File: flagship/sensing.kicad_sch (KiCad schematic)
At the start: 12 parts, among them Q701 2N7002, U11 INA228

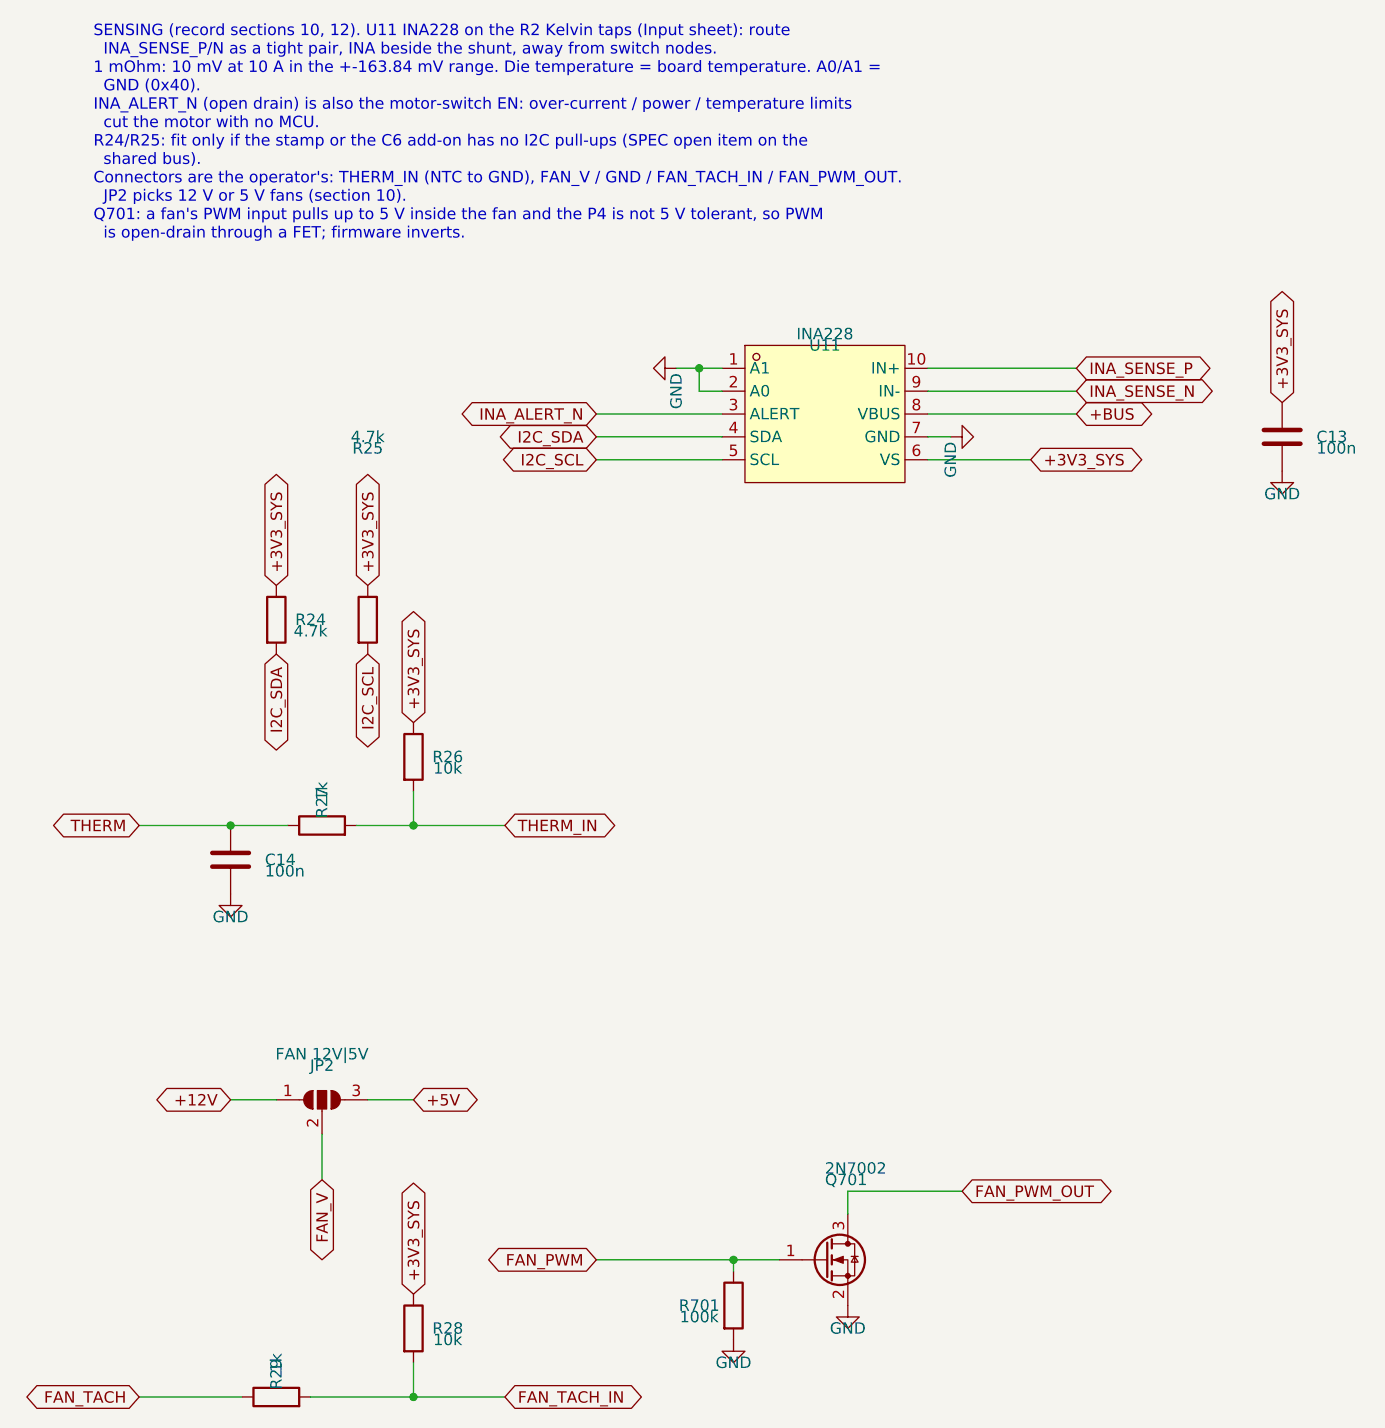
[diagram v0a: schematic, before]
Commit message: flagship: fan supply jumper defaults to 12 V (pre-bridged 1-2, cut and re-bridge for 5 V)
Co-Authored-By: Claude Opus 5.5 (1M context) <noreply@anthropic.com>
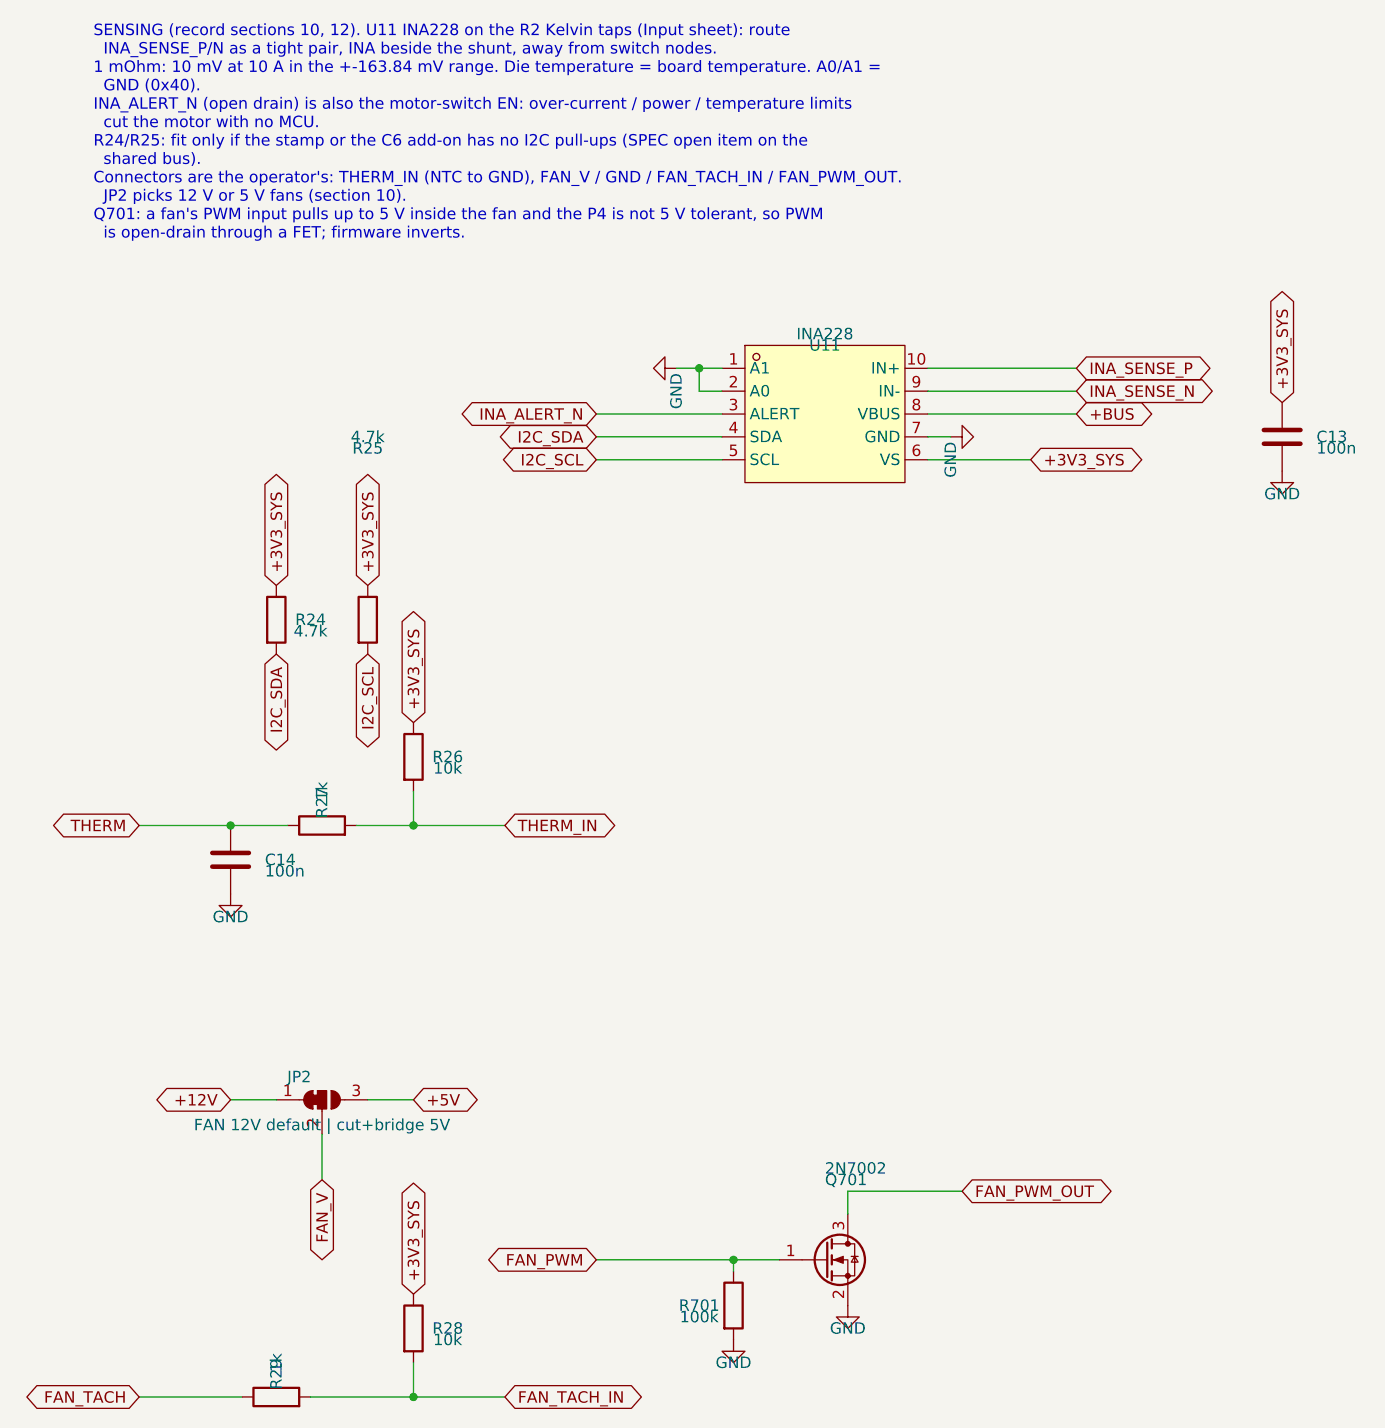
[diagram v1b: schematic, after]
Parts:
- removed JP2: FAN 12V|5V, symbol Jumper:SolderJumper_3_Open
- added JP2: FAN 12V default | cut+bridge 5V, Jumper:SolderJumper-3_P1.3mm_Bridged12_RoundedPad1.0x1.5mm_NumberLabels, symbol Jumper:SolderJumper_3_Bridged12
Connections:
- net +12V: now also JP2.1 (A)
- net +5V: now also JP2.3 (B)
- net FAN_V: now also JP2.2 (C)
